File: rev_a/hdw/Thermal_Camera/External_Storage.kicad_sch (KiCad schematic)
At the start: 37 parts

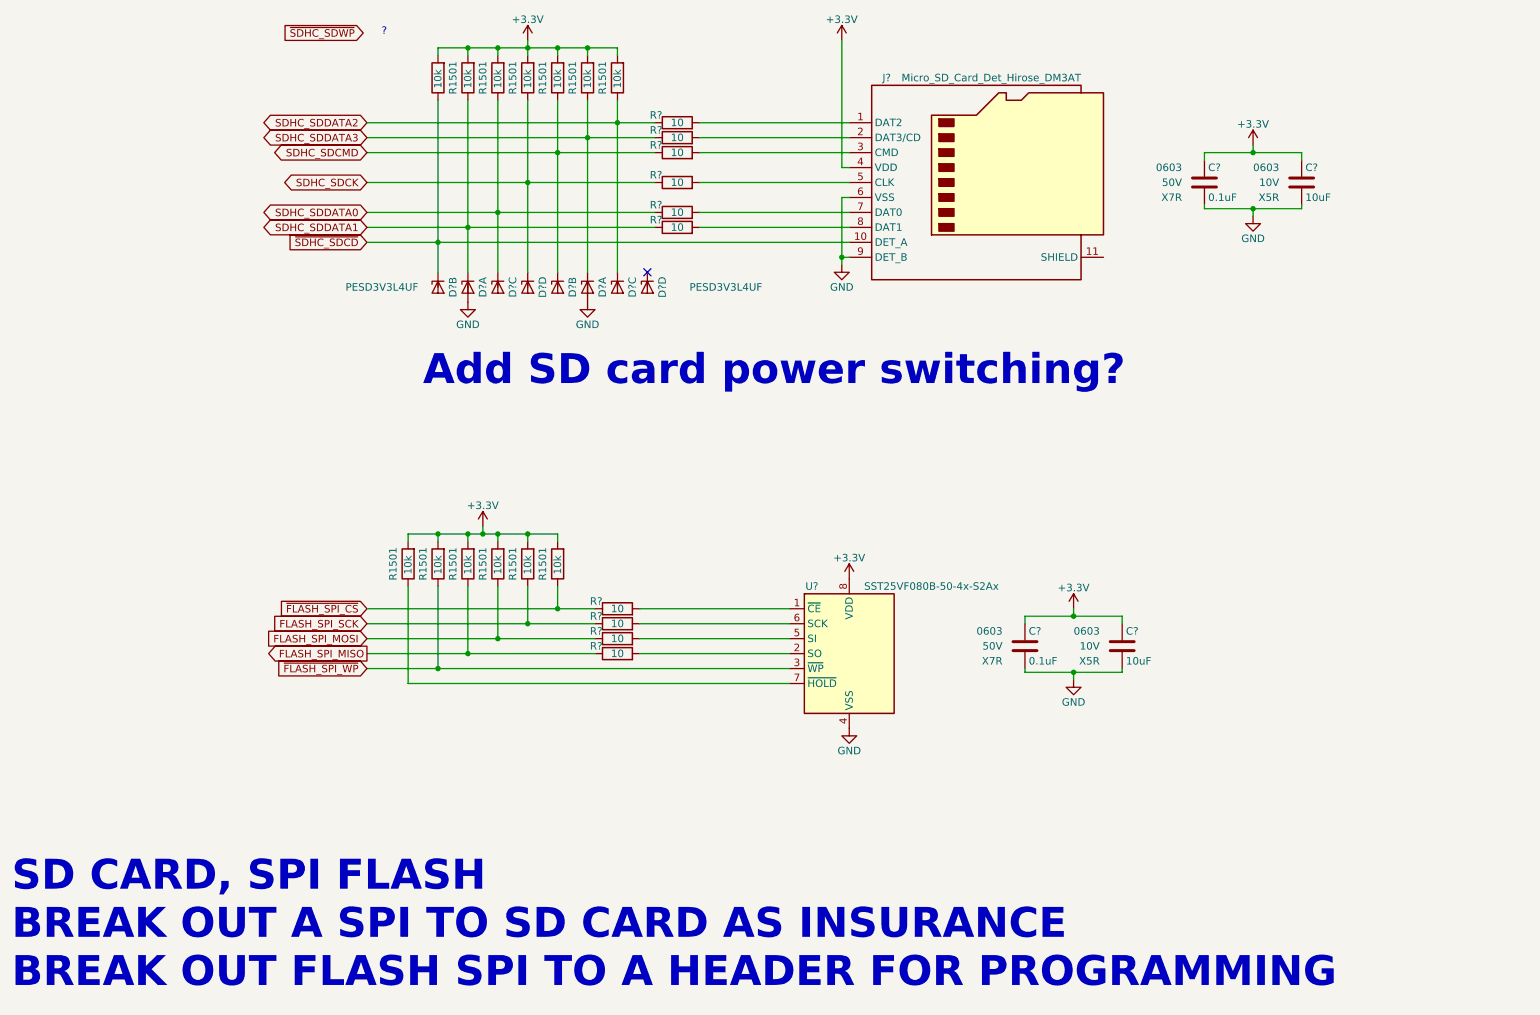
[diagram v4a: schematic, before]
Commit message: changed a lot of circuits from +3.3V to +3.0V VDD
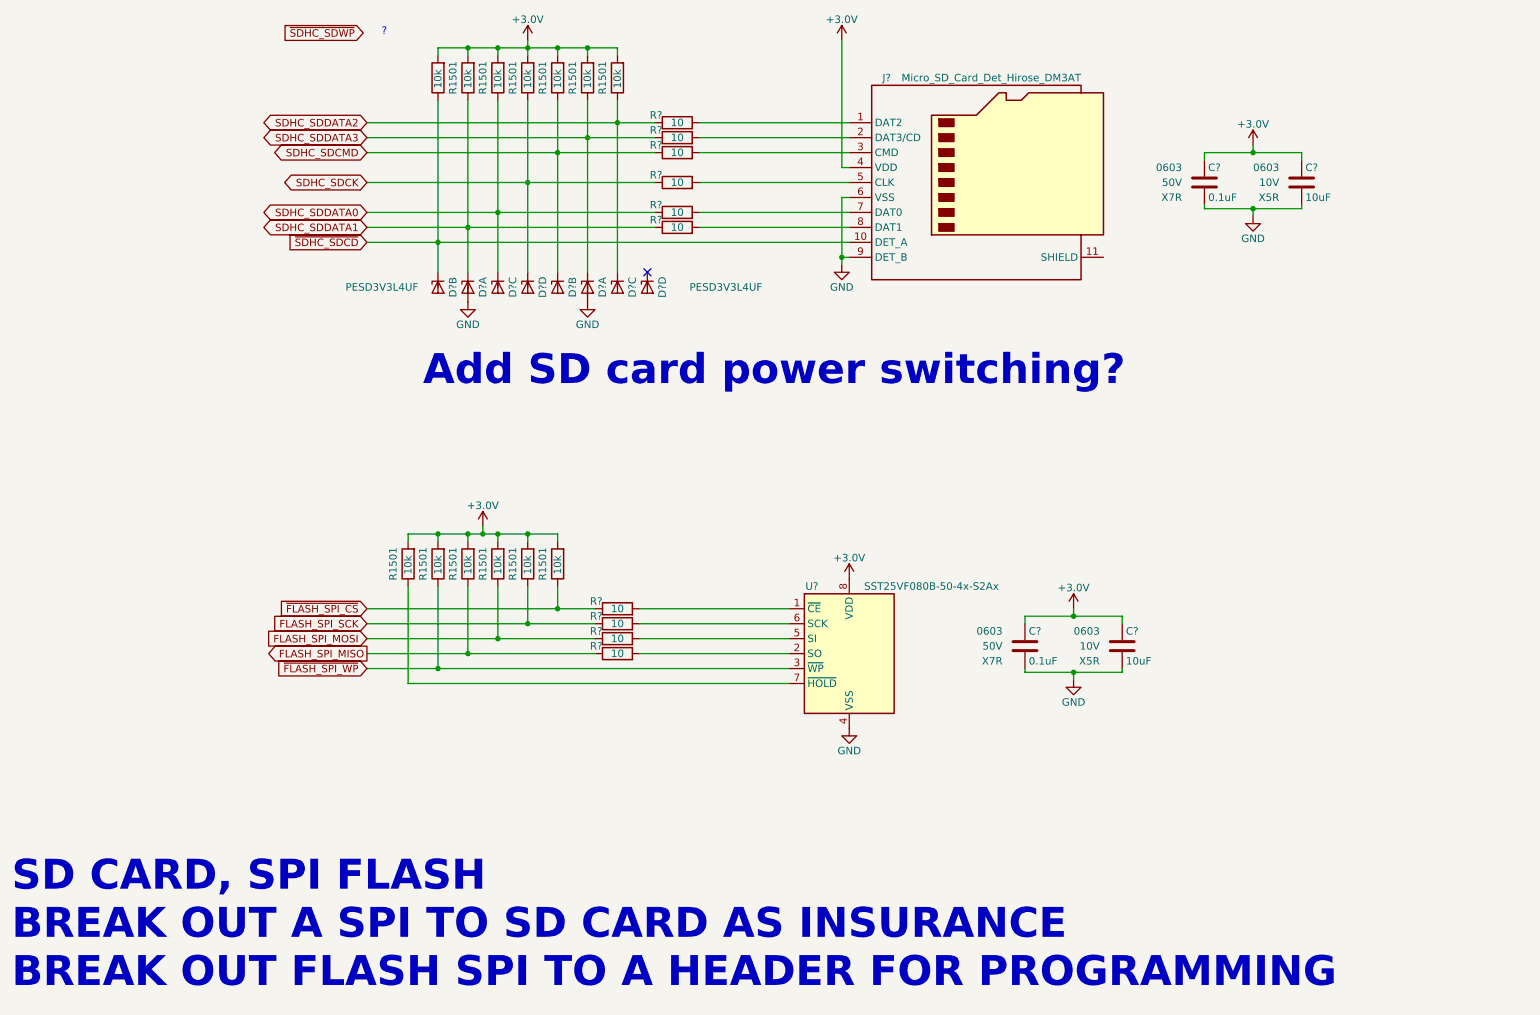
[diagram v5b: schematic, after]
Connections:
- net +3.3V renamed +3.0V

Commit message: duplicated telemetry for all rails, added random tweaks to logic levels of signals
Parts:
- added U?: TPS22810DRV, Package_SON:WSON-6-1EP_2x2mm_P0.65mm_EP1x1.6mm, symbol Power_Management:TPS22810DRV
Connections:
- net +3.0V: no longer C?.1, C?.1, J?.4 (VDD), R1501.1, R1501.1, R1501.1, R1501.1, R1501.1, R1501.1, R1501.1
- new net: U?.4 (GND), U?.7 (GND)
- new net +3.0V_SD: C?.1, C?.1, J?.4 (VDD), R1501.1, R1501.1, R1501.1, R1501.1, R1501.1, R1501.1, R1501.1
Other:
- moved on the sheet: C?, R1501, R?, U?

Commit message: added PIC32 bypass, SD card load switch, other random junk
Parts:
- added C?: 0.1uF, Capacitors_SMD:C_0603, symbol Custom_Library:C_Custom
- added C? (x2): 10uF, Capacitors_SMD:C_0603, symbol Custom_Library:C_Custom
- added R1501: 10k, Resistors_SMD:R_0603, symbol Custom_Library:R_Custom
- added R?: 10, Resistors_SMD:R_0603, symbol Custom_Library:R_Custom
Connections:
- net +3.0V: now also U?.6 (VIN), C?.1
- net +3.0V_SD: now also U?.1 (VOUT), C?.1, R?.1
- net GND: now also U?.4 (GND), U?.7 (GND), C?.2, C?.2, C?.2, R1501.2
- net at U?.2 (QOD): now also R?.2
- net at U?.3 (CT): now also C?.1
- net SD_PWR_EN: now reaches U?.5 (EN/UVLO)
- net SD_PWR_EN: now also R1501.1
- no-connect marks 1 -> 2
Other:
- note removed: "Add SD card power switching?"
- moved on the sheet: C?, D?A, D?B, D?C, D?D, J?, R1501, R?, U?
